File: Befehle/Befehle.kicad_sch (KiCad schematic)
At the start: 77 parts, among them J1 Conn_02x10_Odd_Even, J2 Conn_01x02, J3 Conn_01x04, J4 Conn_02x10_Odd_Even, J5 Conn_01x02, J6 Conn_01x04, U1 74LS14, U2 74LS541, U3 74LS540, U4 74HC139, U5 74HCT373, U6 74HC540, U7 74HCT02, U8 7408, U9 7400

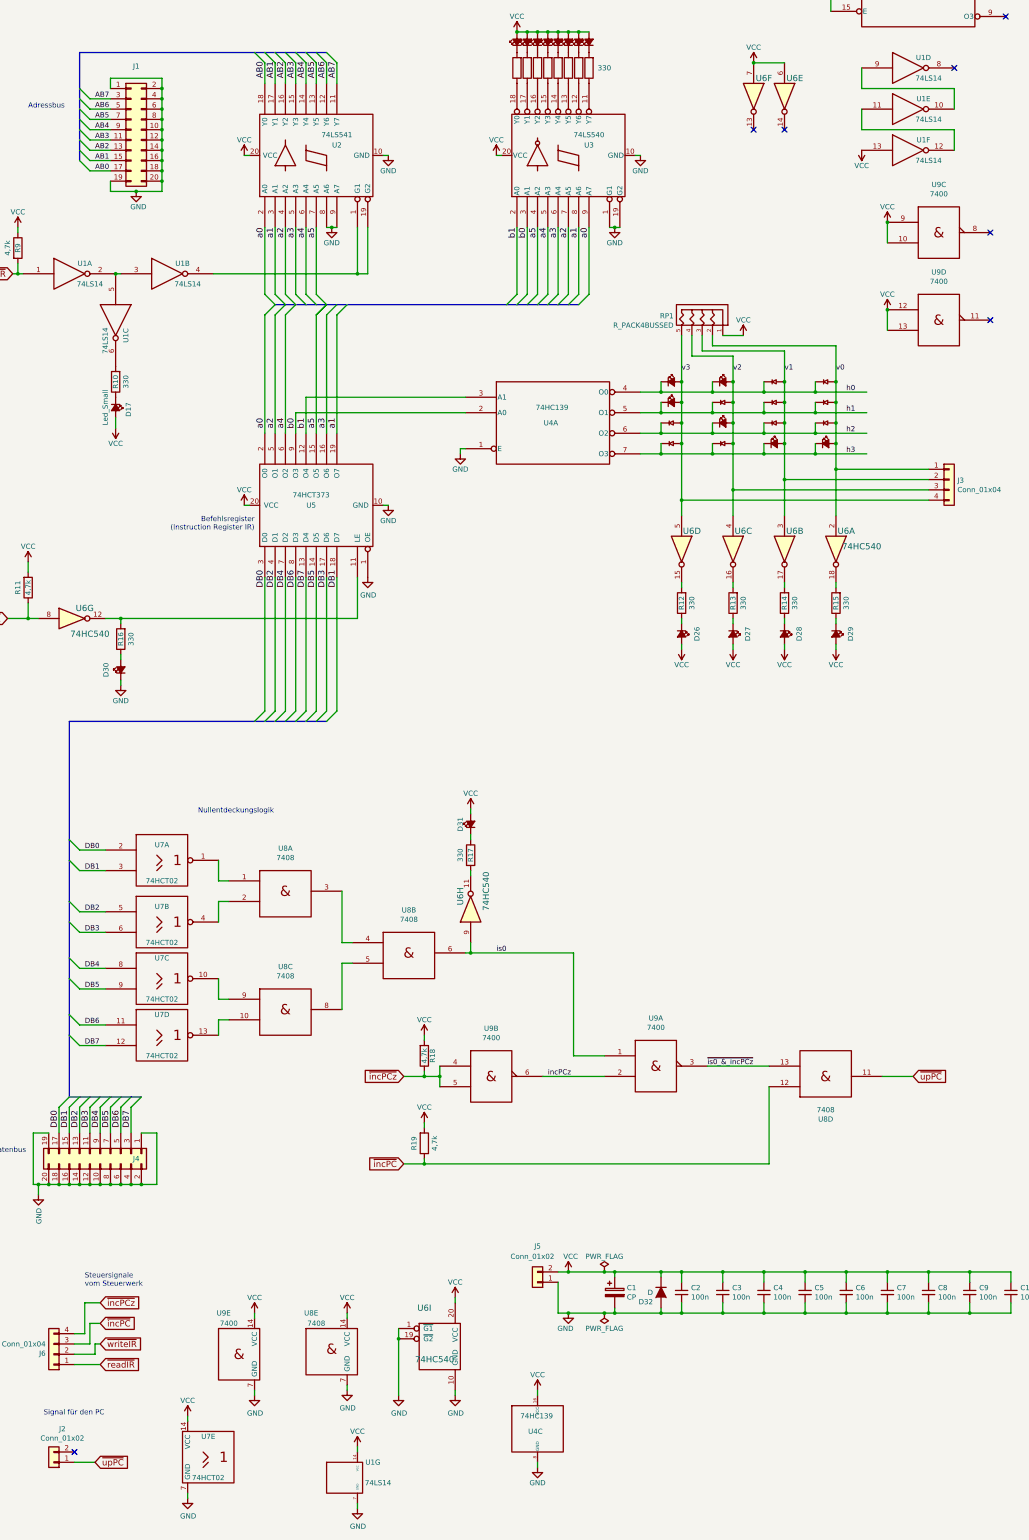
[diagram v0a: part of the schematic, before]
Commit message: - Werte von Bauteilen in den Schaltplänen ergänzt - weitere Hinweise zum Nachbau
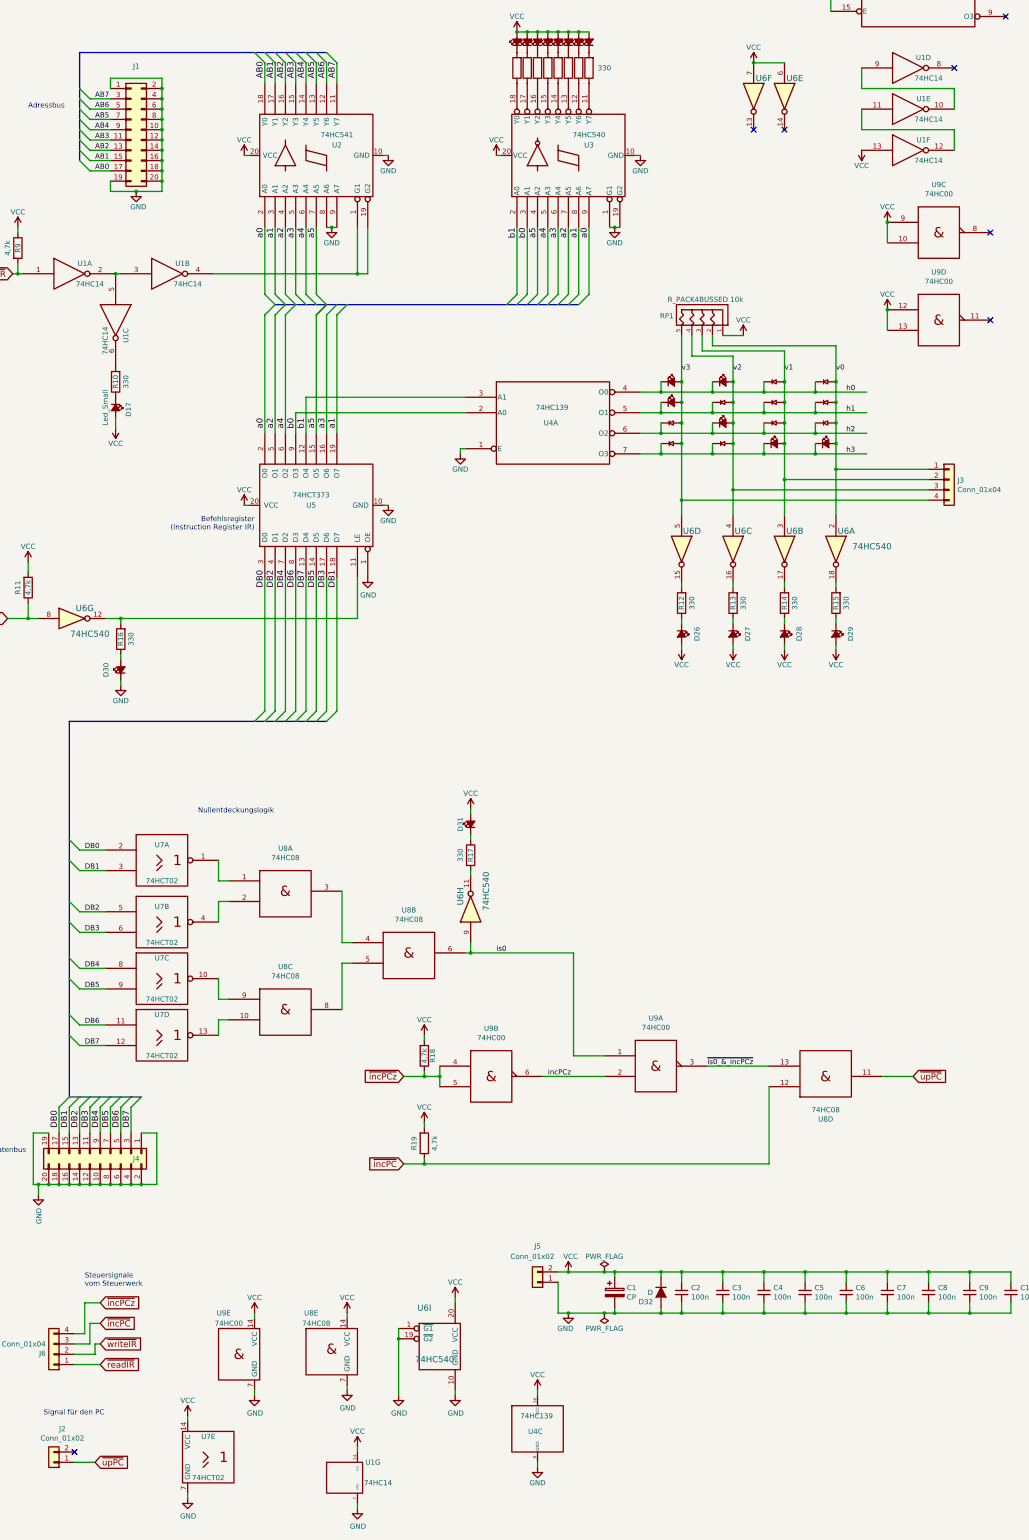
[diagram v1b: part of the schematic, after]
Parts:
- RP1: value R_PACK4BUSSED -> R_PACK4BUSSED 10k
- U1: value 74LS14 -> 74HC14
- U2: value 74LS541 -> 74HC541
- U3: value 74LS540 -> 74HC540
- U8: value 7408 -> 74HC08
- U9: value 7400 -> 74HC00

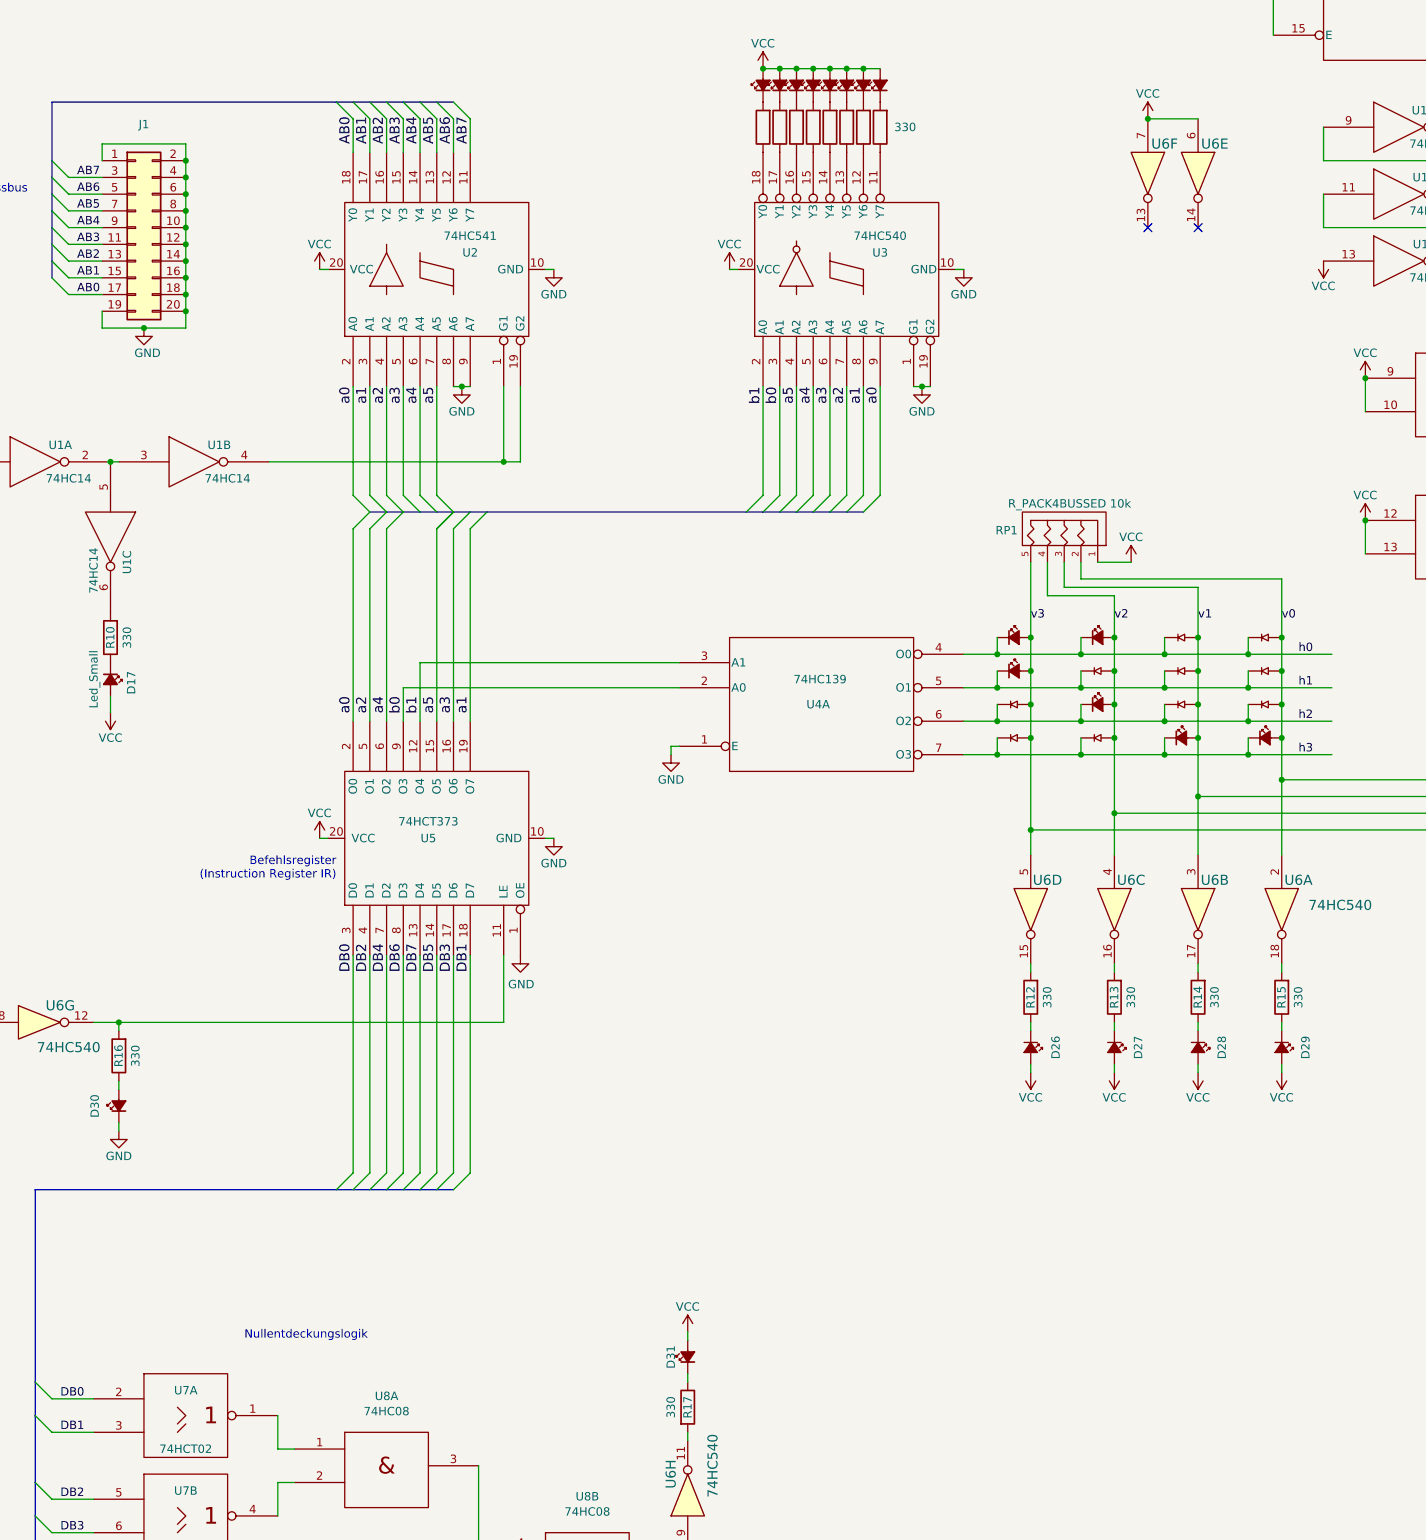
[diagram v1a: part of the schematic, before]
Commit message: Alle Vorwiderstände vor LEDs in 680 Ohm geändert (Issue 5)
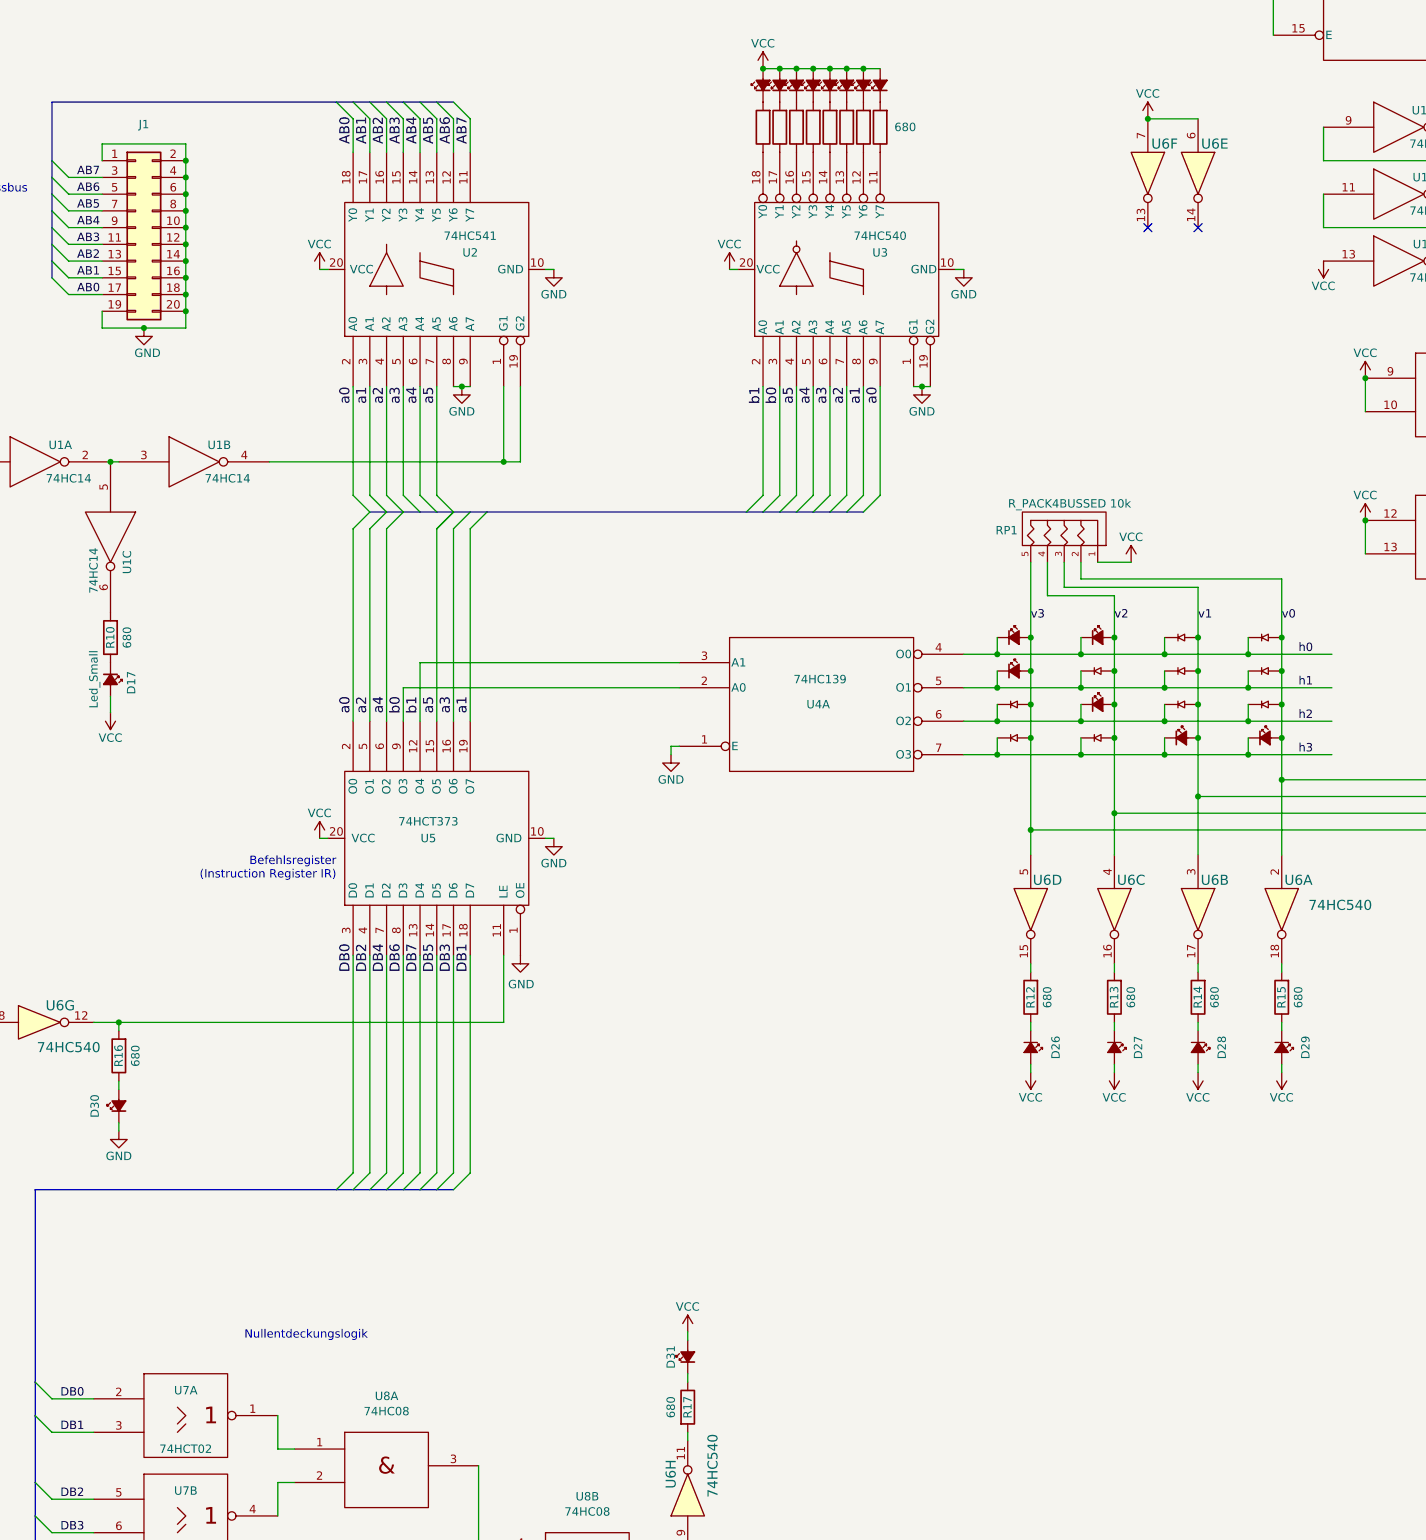
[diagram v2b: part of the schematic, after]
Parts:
- R1, R10, R12, R13, R14, R15, R16, R17, R2, R3, R4, R5, R6, R7, R8: value 330 -> 680
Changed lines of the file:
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@@
       (effects (font (size 1.27 1.27)) hide)
     )
-    (property "Value" "330" (at 154.94 54.61 90)
+    (property "Value" "680" (at 154.94 54.61 90)
       (effects (font (size 1.27 1.27)) hide)
     )
@@
       (effects (font (size 1.27 1.27)) hide)
     )
-    (property "Value" "330" (at 157.48 54.61 90)
+    (property "Value" "680" (at 157.48 54.61 90)
       (effects (font (size 1.27 1.27)) hide)
     )
@@
       (effects (font (size 1.27 1.27)) hide)
     )
-    (property "Value" "330" (at 160.02 54.61 90)
+    (property "Value" "680" (at 160.02 54.61 90)
       (effects (font (size 1.27 1.27)) hide)
     )
@@
       (effects (font (size 1.27 1.27)) hide)
     )
-    (property "Value" "330" (at 162.56 54.61 90)
+    (property "Value" "680" (at 162.56 54.61 90)
       (effects (font (size 1.27 1.27)) hide)
     )
@@
       (effects (font (size 1.27 1.27)) hide)
     )
-    (property "Value" "330" (at 165.1 54.61 90)
+    (property "Value" "680" (at 165.1 54.61 90)
       (effects (font (size 1.27 1.27)) hide)
     )
@@
       (effects (font (size 1.27 1.27)) hide)
     )
-    (property "Value" "330" (at 167.64 54.61 90)
+    (property "Value" "680" (at 167.64 54.61 90)
       (effects (font (size 1.27 1.27)) hide)
     )
@@
       (effects (font (size 1.27 1.27)) hide)
     )
-    (property "Value" "330" (at 170.18 54.61 90)
+    (property "Value" "680" (at 170.18 54.61 90)
       (effects (font (size 1.27 1.27)) hide)
     )
@@
       (effects (font (size 1.27 1.27)) hide)
     )
-    (property "Value" "330" (at 176.53 50.8 0)
+    (property "Value" "680" (at 176.53 50.8 0)
       (effects (font (size 1.27 1.27)))
     )
@@
       (effects (font (size 1.27 1.27)))
     )
-    (property "Value" "330" (at 236.22 182.88 90)
+    (property "Value" "680" (at 236.22 182.88 90)
       (effects (font (size 1.27 1.27)))
     )
@@
       (effects (font (size 1.27 1.27)))
     )
-    (property "Value" "330" (at 223.52 182.88 90)
+    (property "Value" "680" (at 223.52 182.88 90)
       (effects (font (size 1.27 1.27)))
     )
@@
       (effects (font (size 1.27 1.27)))
     )
-    (property "Value" "330" (at 210.82 182.88 90)
+    (property "Value" "680" (at 210.82 182.88 90)
       (effects (font (size 1.27 1.27)))
     )
@@
       (effects (font (size 1.27 1.27)))
     )
-    (property "Value" "330" (at 198.12 182.88 90)
+    (property "Value" "680" (at 198.12 182.88 90)
       (effects (font (size 1.27 1.27)))
     )
@@
       (effects (font (size 1.27 1.27)))
     )
-    (property "Value" "330" (at 58.42 128.27 90)
+    (property "Value" "680" (at 58.42 128.27 90)
       (effects (font (size 1.27 1.27)))
     )
@@
       (effects (font (size 1.27 1.27)))
     )
-    (property "Value" "330" (at 140.97 245.11 90)
+    (property "Value" "680" (at 140.97 245.11 90)
       (effects (font (size 1.27 1.27)))
     )
@@
       (effects (font (size 1.27 1.27)))
     )
-    (property "Value" "330" (at 59.69 191.77 90)
-      (effects (font (size 1.27 1.27)))
-    )
+    (property "Value" "680" (at 59.69 191.77 90)
+      (effects (font (size 1.27 1.27)))
+    )
